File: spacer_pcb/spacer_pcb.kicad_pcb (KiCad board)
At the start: 2 copper layers, 9.4 x 38.2 mm, 3 parts, among them J1 Conn_01x15, J2 Conn_02x15_Odd_Even, J3 Conn_01x15

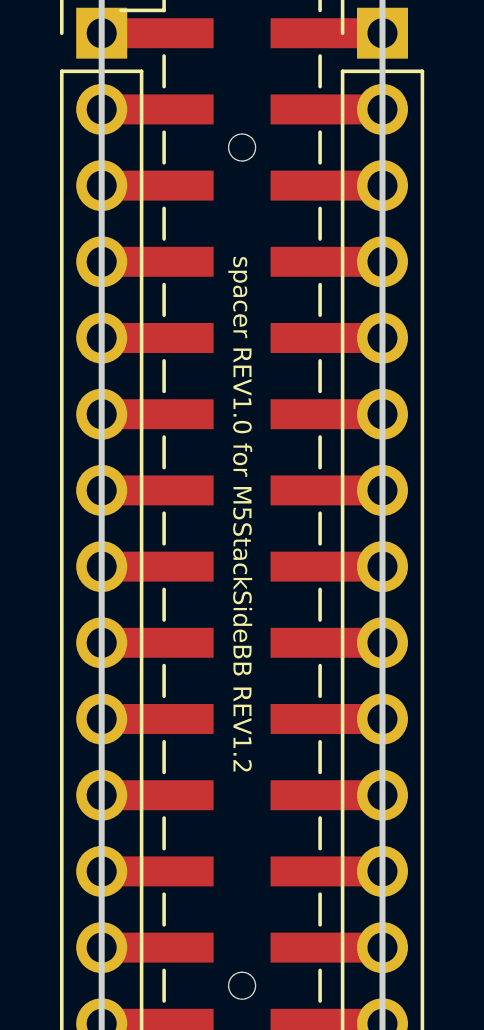
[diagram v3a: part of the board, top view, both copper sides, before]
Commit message: Correct revision of spacer_pcb
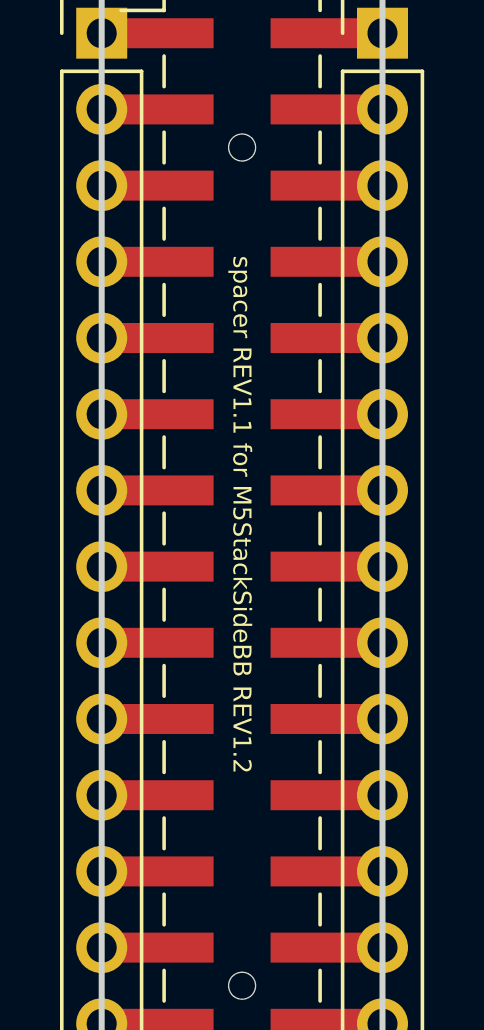
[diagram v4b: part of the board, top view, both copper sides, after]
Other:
- board text added: "spacer REV1.1 for M5StackSideBB REV1.2"
- board text removed: "spacer REV1.0 for M5StackSideBB REV1.2"
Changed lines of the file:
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@@
     )
   )
-  (gr_text "spacer REV1.0 for M5StackSideBB REV1.2" (at 135.89 79.6036 270) (layer F.SilkS)
+  (gr_text "spacer REV1.1 for M5StackSideBB REV1.2" (at 135.89 79.6036 270) (layer F.SilkS)
     (effects (font (size 0.6 0.6) (thickness 0.15)))
   )

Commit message: Update design for production
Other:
- board text added: "spacer REV1.1 for M5StackSideBB Rev 2018.08"
- board text removed: "spacer REV1.1 for M5StackSideBB REV1.2"
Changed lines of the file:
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@@
-(kicad_pcb (version 20171130) (host pcbnew 5.0.0-fee4fd1~65~ubuntu17.10.1)
+(kicad_pcb (version 20171130) (host pcbnew 5.0.1-33cea8e~67~ubuntu18.04.1)
   (general
     (thickness 1.6)
@@
     (pad_drill 0.762)
     (pad_to_mask_clearance 0.2)
+    (solder_mask_min_width 0.25)
     (aux_axis_origin 0 0)
     (visible_elements FFFFFF7F)
@@
     )
   )
-  (gr_text "spacer REV1.1 for M5StackSideBB REV1.2" (at 135.89 79.6036 270) (layer F.SilkS)
+  (gr_text "spacer REV1.1 for M5StackSideBB Rev 2018.08" (at 135.89 79.6036 270) (layer F.SilkS)
     (effects (font (size 0.6 0.6) (thickness 0.15)))
   )

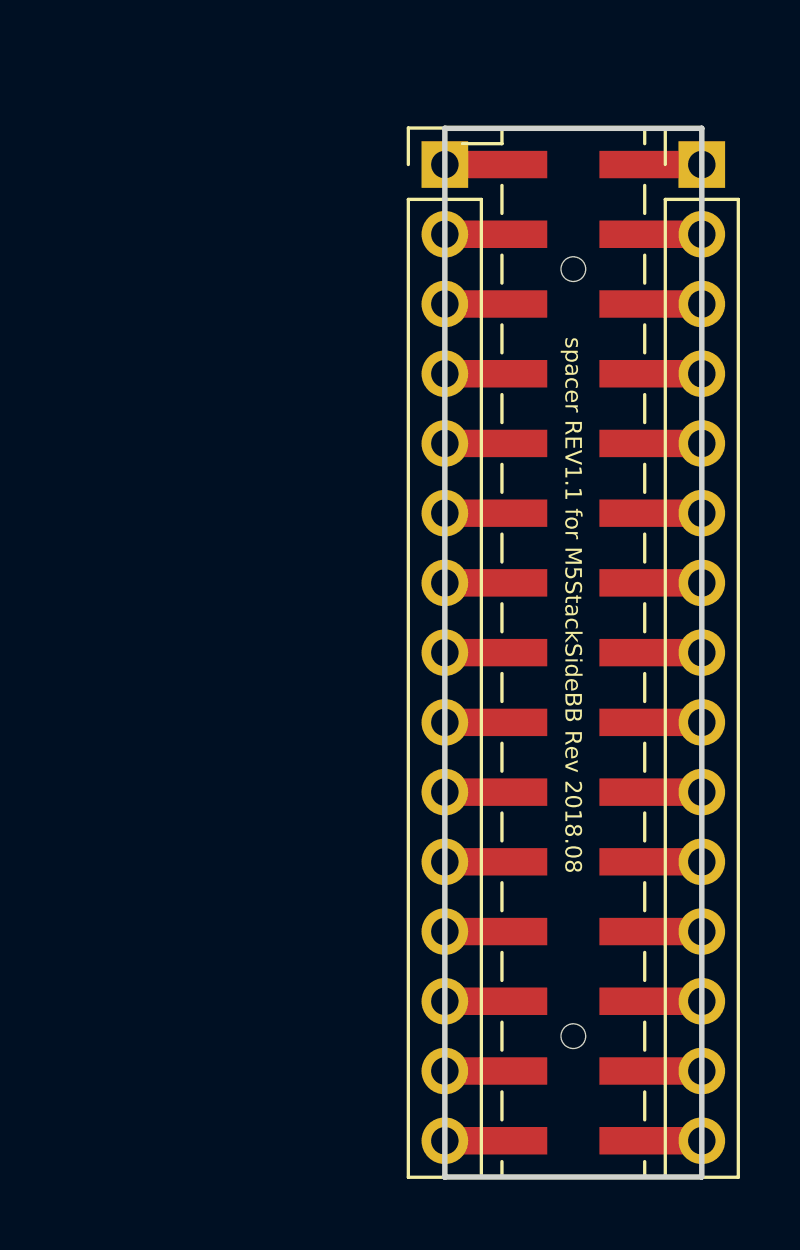
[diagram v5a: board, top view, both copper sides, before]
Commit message: Remove redundant info from spacer pcb
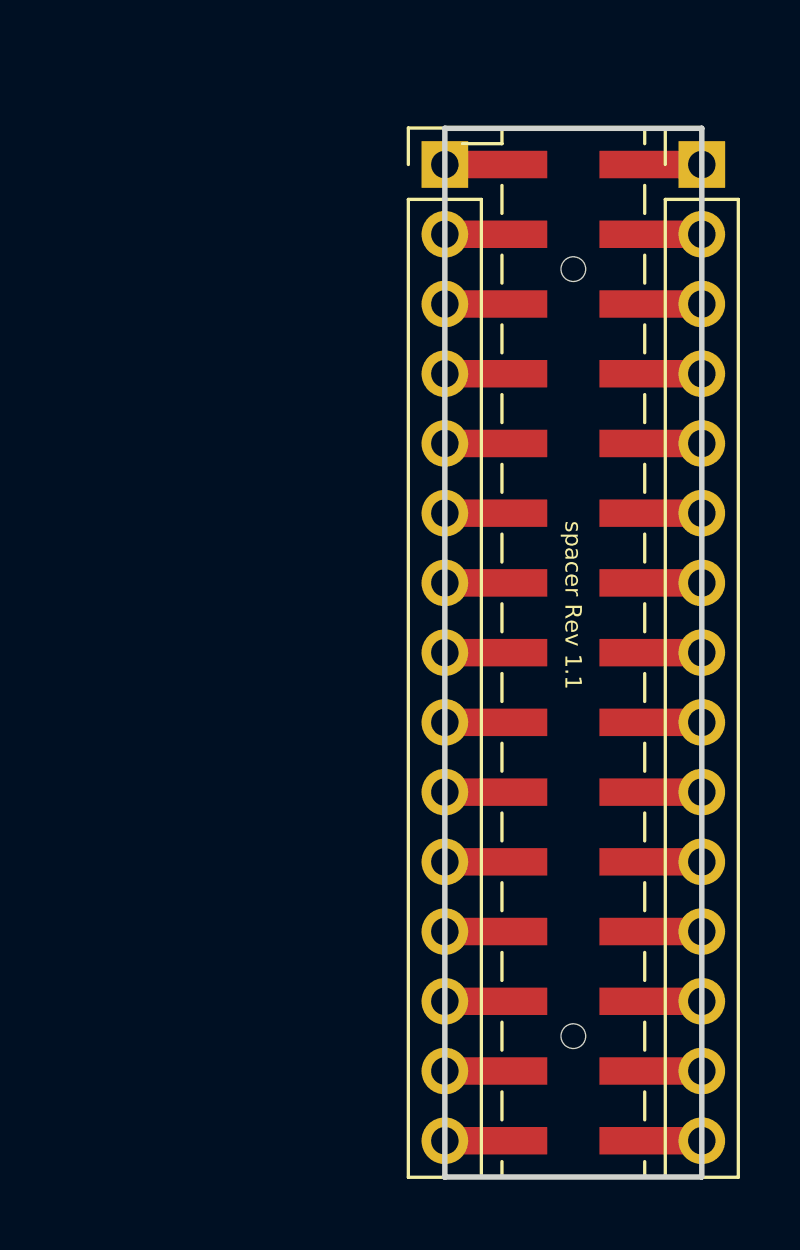
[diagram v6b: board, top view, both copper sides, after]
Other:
- board text added: "spacer Rev 1.1"
- board text removed: "spacer REV1.1 for M5StackSideBB Rev 2018.08"
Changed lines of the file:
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@@
-(kicad_pcb (version 20171130) (host pcbnew 5.0.1-33cea8e~67~ubuntu18.04.1)
+(kicad_pcb (version 20171130) (host pcbnew 5.0.2-bee76a0~70~ubuntu18.04.1)
   (general
     (thickness 1.6)
@@
     )
   )
-  (gr_text "spacer REV1.1 for M5StackSideBB Rev 2018.08" (at 135.89 79.6036 270) (layer F.SilkS)
+  (gr_text "spacer Rev 1.1" (at 135.89 79.6036 270) (layer F.SilkS)
     (effects (font (size 0.6 0.6) (thickness 0.15)))
   )

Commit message: Add bottom pads for spacer PCB
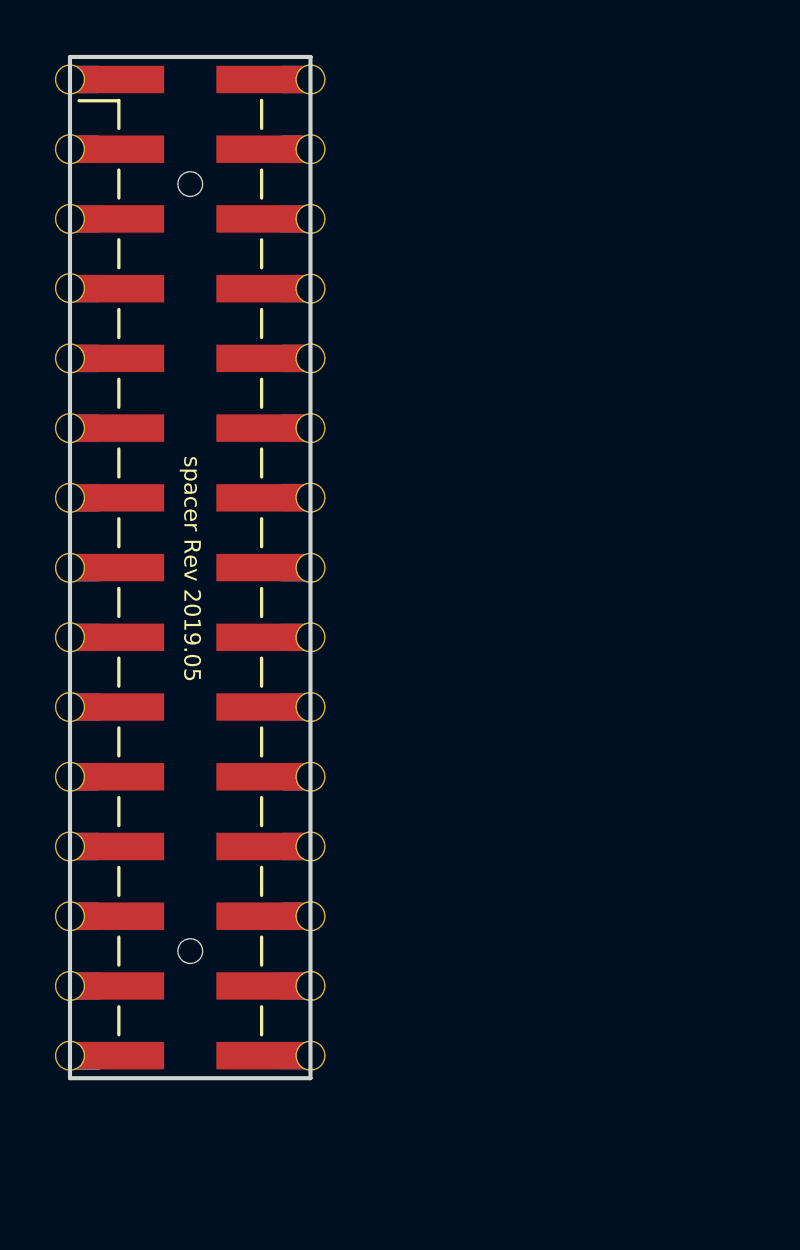
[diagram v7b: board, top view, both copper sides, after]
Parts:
- removed J1, J3: Conn_01x15, Connector_PinHeader_2.54mm:PinHeader_1x15_P2.54mm_Vertical
- J2: footprint footprints:PinHeader_2x15_P2.54mm_Vertical_SMD_for_M5Stack -> footprints:PinHeader_2x15_P2.54mm_M5Stack_SpacerPCB
- moved J2 14.3 mm to (121.9, 78.2)
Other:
- board size 9.4 x 38.2 mm -> 8.8 x 37.2 mm
- board text added: "spacer Rev 2019.05"
- board text removed: "spacer Rev 1.1"

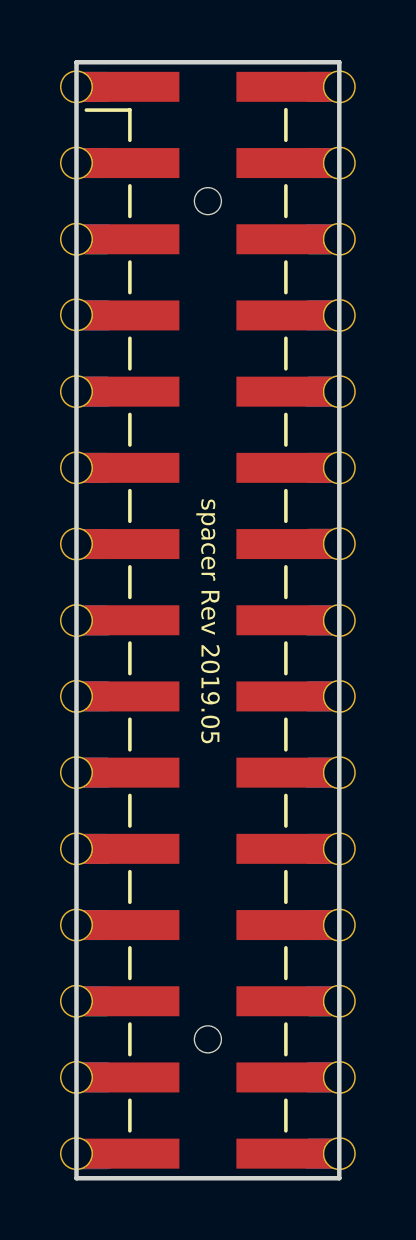
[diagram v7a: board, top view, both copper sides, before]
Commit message: Update as narrow long style for pcb to spacer pads
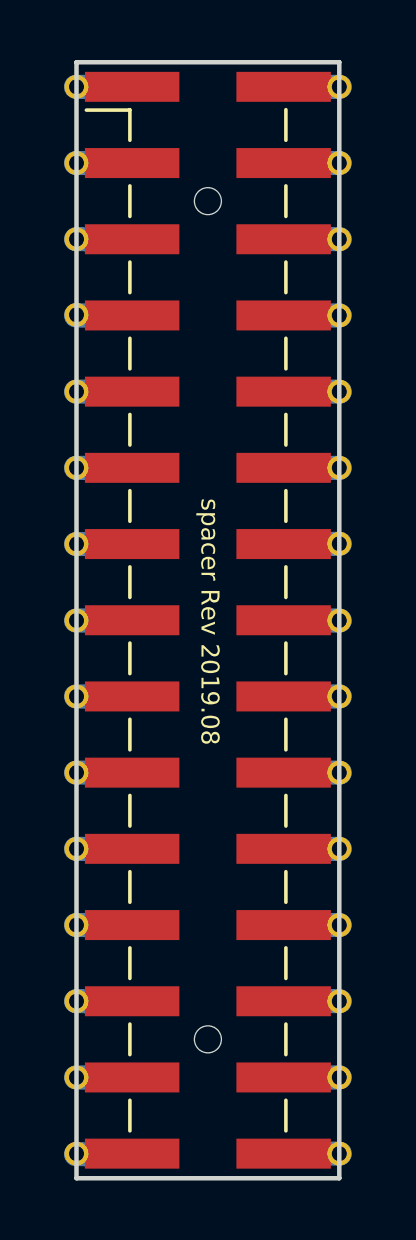
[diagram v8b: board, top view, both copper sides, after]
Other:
- board text added: "spacer Rev 2019.08"
- board text removed: "spacer Rev 2019.05"
